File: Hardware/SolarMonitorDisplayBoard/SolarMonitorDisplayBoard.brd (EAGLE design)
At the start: 100 x 57 mm, 7 parts

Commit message: Add some labels.
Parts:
- added BARO: T5403_BREAKOUT, BtParts:T5403_BREAKOUT
- U$3: value T5403_BREAKOUT -> (none); device BtParts:T5403_BREAKOUT -> SparkFun-Aesthetics:OSHW-LOGO-L
- moved U$3 69.2 mm to (49.5, 5.08), turned to 0 degrees
- renumbered U$4 to TEMP
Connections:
- net FONA_KEY renamed TEMP
- net GND: now also BARO.1; no longer U$3.1
- net SCL: now also BARO.3; no longer U$3.3
- net SDA: now also BARO.4; no longer U$3.4
- net VCC: now also BARO.2; no longer U$3.2
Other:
- board text added: "BT SolarMonitor Display"
- board text added: "rev A"
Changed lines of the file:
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@@
 <grid distance="0.05" unitdist="inch" unit="mil" style="lines" multiple="1" display="no" altdistance="0.025" altunitdist="inch" altunit="mil"/>
 <layers>
-<layer number="1" name="Top" color="4" fill="1" visible="no" active="yes"/>
+<layer number="1" name="Top" color="4" fill="1" visible="yes" active="yes"/>
 <layer number="16" name="Bottom" color="1" fill="1" visible="yes" active="yes"/>
 <layer number="17" name="Pads" color="2" fill="1" visible="yes" active="yes"/>
@@
 <wire x1="100" y1="57" x2="0" y2="57" width="0" layer="20"/>
 <wire x1="0" y1="57" x2="0" y2="0" width="0" layer="20"/>
+<text x="7.62" y="1.27" size="1.778" layer="22" rot="MR0">rev A</text>
+<text x="2.54" y="53.34" size="1.778" layer="21" font="vector">BT SolarMonitor Display</text>
 </plain>
 <attributes>
@@
 <element name="U$1" library="BtParts" package="NOKIA_LCD_BREAKOUT" value="NOKIA_LCD_BREAKOUT" x="2.54" y="7.62"/>
 <element name="U$2" library="BtParts" package="NOKIA_LCD_BREAKOUT" value="NOKIA_LCD_BREAKOUT" x="54.61" y="7.62"/>
-<element name="MS1" library="BtParts" package="FONA" value="FONA" x="3.175" y="15.24" rot="MR90"/>
+<element name="MS1" library="BtParts" package="FONA" value="FONA" x="3.175" y="15.24" smashed="yes" rot="MR90"/>
 <element name="J1" library="SparkFun-Connectors" package="2X10" value="" x="62.865" y="29.845"/>
 <element name="JP1" library="SparkFun-Passives" package="PAD-JUMPER-2-NO_NO_SILK" value="JUMPER-PAD-2-NO" x="7.62" y="33.02" rot="MR90"/>
-<element name="U$3" library="BtParts" package="T5403_BREAKOUT" value="T5403_BREAKOUT" x="97.79" y="54.61" rot="MR270"/>
-<element name="U$4" library="BtParts" package="MCP9808_BREAKOUT" value="MCP9808_BREAKOUT" x="97.79" y="22.86" rot="MR270"/>
+<element name="BARO" library="BtParts" package="T5403_BREAKOUT" value="T5403_BREAKOUT" x="97.79" y="54.61" rot="MR270"/>
+<element name="TEMP" library="BtParts" package="MCP9808_BREAKOUT" value="MCP9808_BREAKOUT" x="97.79" y="22.86" rot="MR270"/>
+<element name="U$3" library="SparkFun-Aesthetics" package="OSHW-LOGO-L" value="" x="49.53" y="5.08" rot="MR0"/>
 </elements>
 <signals>
@@
 <via x="5.08" y="45.72" extent="1-16" drill="0.6" shape="octagon"/>
 <via x="5.08" y="5.08" extent="1-16" drill="0.6" shape="octagon"/>
-<contactref element="U$3" pad="1"/>
-<contactref element="U$4" pad="2"/>
+<contactref element="BARO" pad="1"/>
+<contactref element="TEMP" pad="2"/>
 <contactref element="MS1" pad="2"/>
 <via x="19.685" y="13.335" extent="1-16" drill="0.6" shape="octagon"/>
@@
 <wire x1="26.035" y1="43.18" x2="29.845" y2="40.005" width="0.6096" layer="16"/>
 <wire x1="29.845" y1="40.005" x2="29.845" y2="12.7" width="0.6096" layer="16"/>
-<contactref element="U$3" pad="2"/>
-<contactref element="U$4" pad="1"/>
+<contactref element="BARO" pad="2"/>
+<contactref element="TEMP" pad="1"/>
 <wire x1="53.975" y1="28.575" x2="53.975" y2="14.605" width="0.6096" layer="16"/>
 <wire x1="53.975" y1="14.605" x2="52.07" y2="12.7" width="0.6096" layer="16"/>
@@
 <signal name="SCL">
 <contactref element="J1" pad="18"/>
-<contactref element="U$3" pad="3"/>
-<contactref element="U$4" pad="3"/>
+<contactref element="BARO" pad="3"/>
+<contactref element="TEMP" pad="3"/>
 <wire x1="71.755" y1="31.115" x2="71.755" y2="34.29" width="0.254" layer="16"/>
 <wire x1="71.755" y1="34.29" x2="73.66" y2="36.195" width="0.254" layer="16"/>
@@
 <signal name="SDA">
 <contactref element="J1" pad="20"/>
-<contactref element="U$3" pad="4"/>
-<contactref element="U$4" pad="4"/>
+<contactref element="BARO" pad="4"/>
+<contactref element="TEMP" pad="4"/>
 <wire x1="74.295" y1="31.115" x2="74.295" y2="34.29" width="0.254" layer="16"/>
 <wire x1="74.295" y1="34.29" x2="91.44" y2="43.18" width="0.254" layer="16"/>
@@
 <wire x1="59.055" y1="26.035" x2="59.055" y2="28.575" width="0.6096" layer="1"/>
 </signal>
-<signal name="FONA_KEY">
+<signal name="TEMP">
 <contactref element="J1" pad="9"/>
 <contactref element="MS1" pad="7"/>

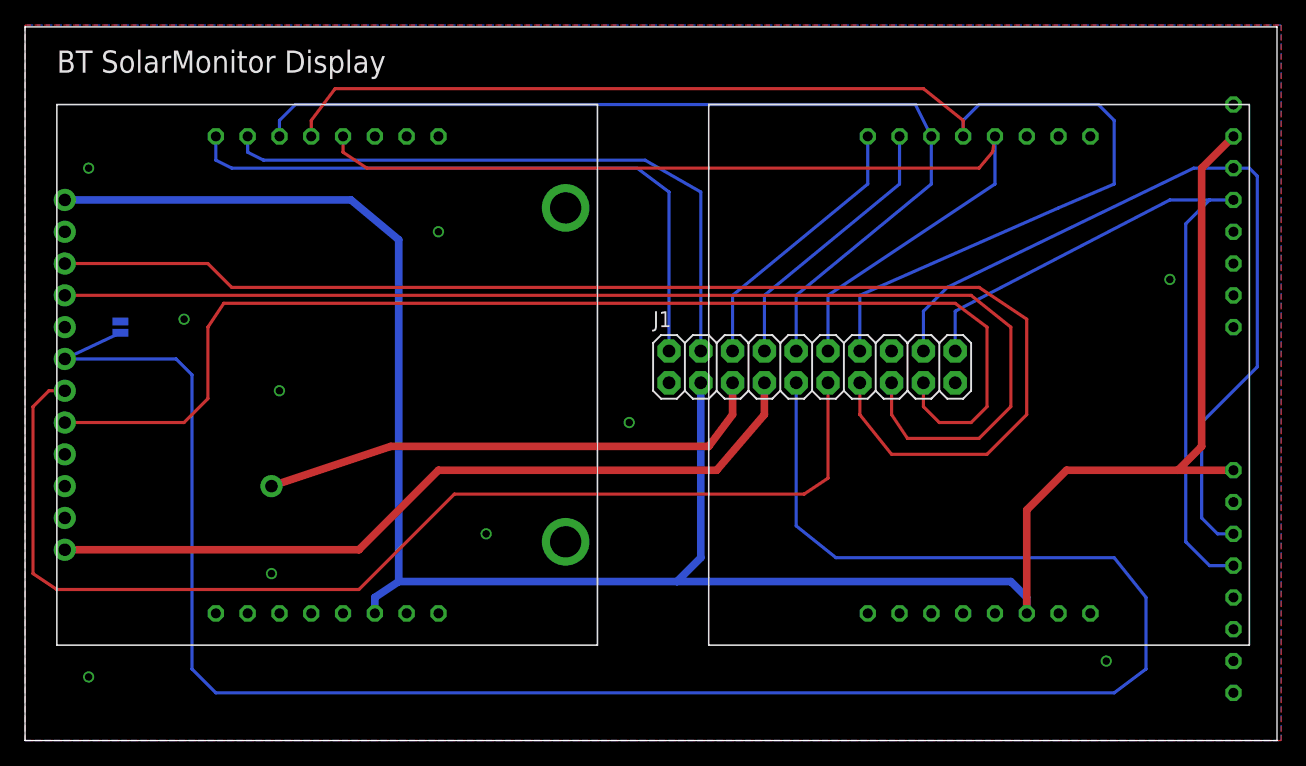
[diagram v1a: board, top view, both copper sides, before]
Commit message: Add trim pot and button for background light.
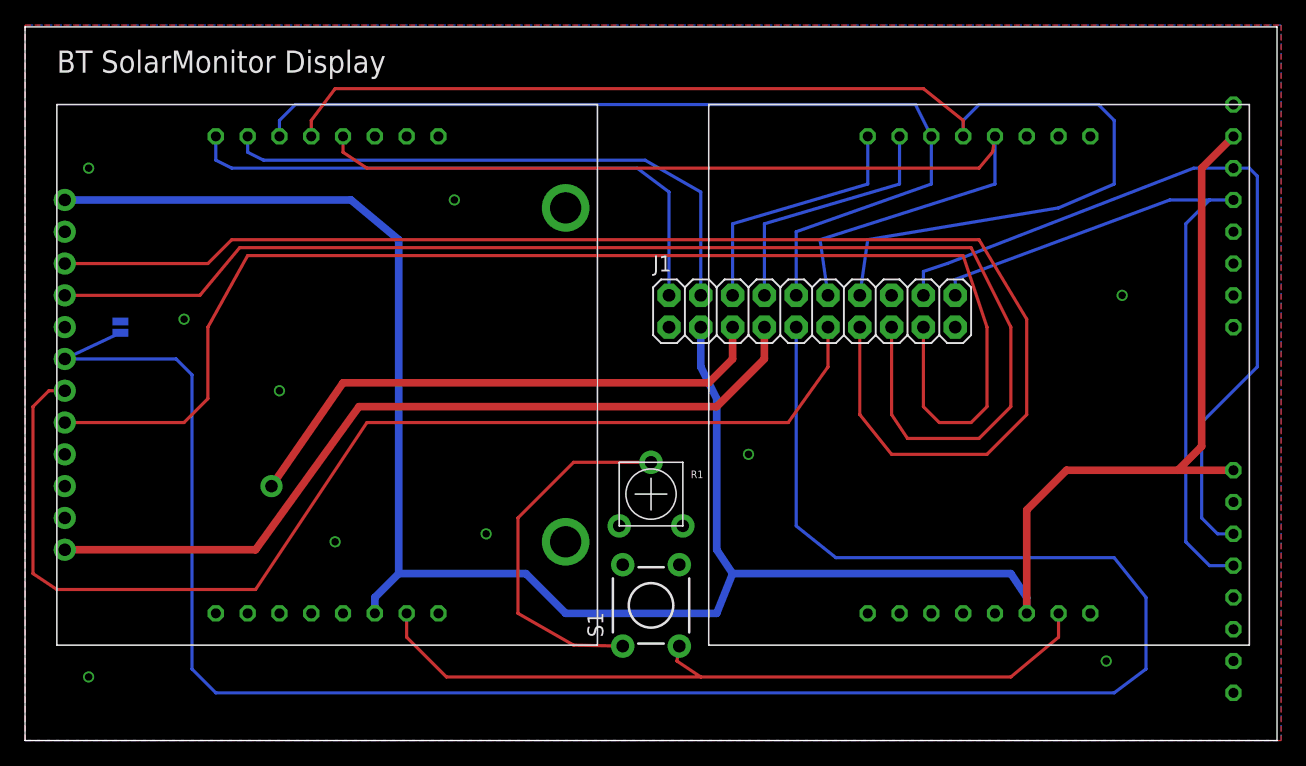
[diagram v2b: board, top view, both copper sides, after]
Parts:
- added R1: (no value), SparkFun-Electromechanical:TRIM_POT_PTH
- added S1: SWITCH-MOMENTARY-2PTH, SparkFun-Electromechanical:TACTILE-PTH
- moved J1 4.45 mm to (62.9, 34.3)
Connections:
- new net N$1: R1.2, S1.1
- new net N$2: S1.3, U$1.P$7, U$2.P$7
- net GND: now also R1.1
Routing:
- net N$2: track 0.00 -> 61.8 mm
- net N$1: track 0.00 -> 29.1 mm
- net FONA_RST: track 96.2 -> 106.5 mm
- net FONATX: track 96.9 -> 106.2 mm
- net VCC: track 181.9 -> 189.3 mm
- net FONARX: track 104.7 -> 112.0 mm
- net DISP2_RST: track 51.6 -> 47.1 mm
- net DISP2_CE: track 51.0 -> 46.5 mm
- net TEMP: track 164.2 -> 168.7 mm
- net 5V: track 41.2 -> 44.5 mm
- net SDA: track 60.3 -> 57.3 mm
- net FONA_BAT: track 63.1 -> 65.8 mm
- net SCL: track 65.3 -> 62.6 mm
- net DISP_DC: track 77.7 -> 75.8 mm
- net MOSI: track 102.9 -> 101.0 mm
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
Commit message: Work in progress.
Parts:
- moved U$3 41.9 mm to (91.4, 3.81)
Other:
- board text added: "bittailor - SolarMonitor Display Board - rev A"
- board text removed: "rev A"
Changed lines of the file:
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@@
 <wire x1="100" y1="57" x2="0" y2="57" width="0" layer="20"/>
 <wire x1="0" y1="57" x2="0" y2="0" width="0" layer="20"/>
-<text x="7.62" y="1.27" size="1.778" layer="22" rot="MR0">rev A</text>
+<text x="86.36" y="1.27" size="1.27" layer="22" font="vector" rot="MR0">bittailor - SolarMonitor Display Board - rev A</text>
 <text x="2.54" y="53.34" size="1.778" layer="21" font="vector">BT SolarMonitor Display</text>
 </plain>
@@
 <element name="BARO" library="BtParts" package="T5403_BREAKOUT" value="T5403_BREAKOUT" x="97.79" y="54.61" rot="MR270"/>
 <element name="TEMP" library="BtParts" package="MCP9808_BREAKOUT" value="MCP9808_BREAKOUT" x="97.79" y="22.86" rot="MR270"/>
-<element name="U$3" library="SparkFun-Aesthetics" package="OSHW-LOGO-L" value="" x="49.53" y="5.08" rot="MR0"/>
+<element name="U$3" library="SparkFun-Aesthetics" package="OSHW-LOGO-L" value="" x="91.44" y="3.81" rot="MR0"/>
 <element name="R1" library="SparkFun-Electromechanical" package="TRIM_POT_PTH" value="" x="50" y="19.685"/>
 <element name="S1" library="SparkFun-Electromechanical" package="TACTILE-PTH" value="SWITCH-MOMENTARY-2PTH" x="50" y="10.795" rot="R90">
